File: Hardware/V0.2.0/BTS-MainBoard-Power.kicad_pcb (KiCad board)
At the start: 4 copper layers, 100 x 100 mm, 62 parts, among them J10 PeCon, J11 PeCon, J12 FanConn, J13 FanConn, J14 FanConn, J15 FanConn, J16 FanConn, J17 FanConn, J18 FanConn, J19 FanConn, J3 LogicBoardConnector, J4 PeCon, J5 PeCon, J6 PeCon, J7 PeCon, J8 PeCon, J9 PeCon, Q1 DMG3418L, Q2 NTMFS5H419NL, Q3 NTMFS5H419NL, Q4 NTMFS5H419NL, Q5 NTMFS5H419NL, U1 LM5109BMA, U2 LM5109BMA

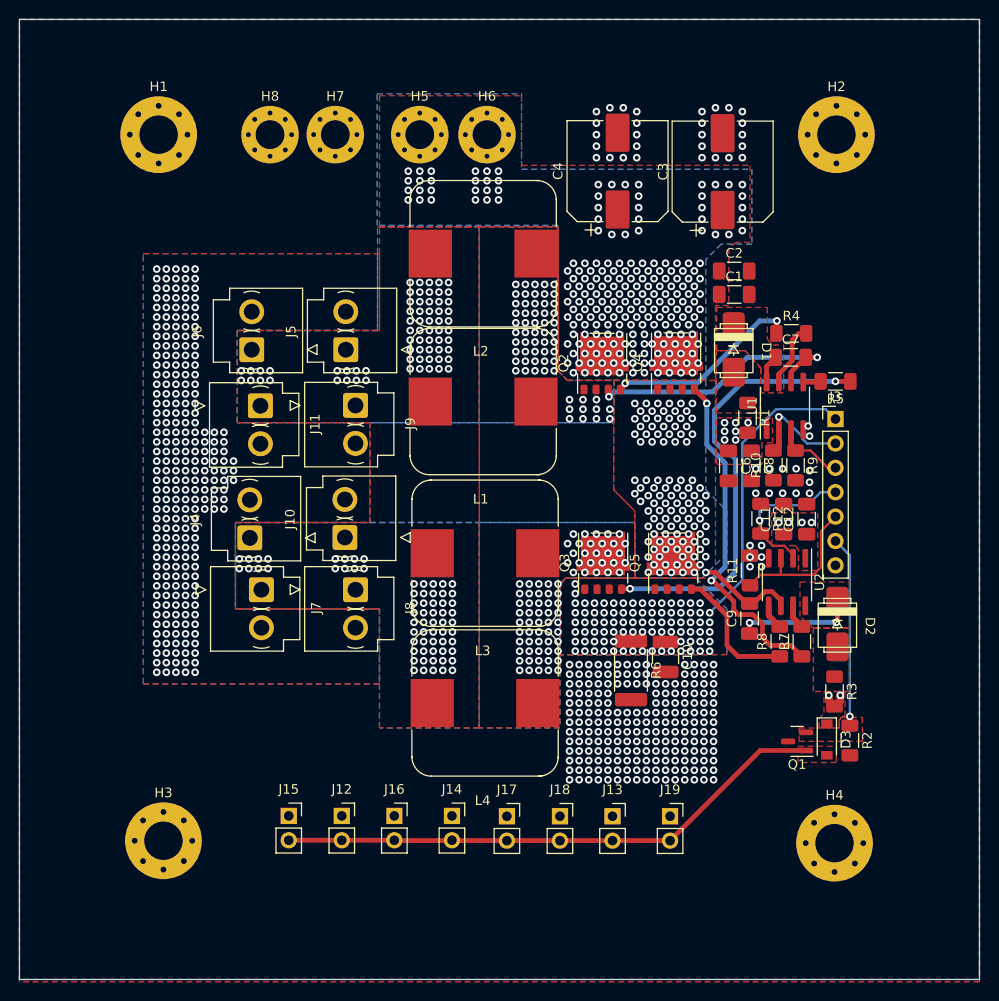
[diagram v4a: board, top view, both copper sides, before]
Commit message: Redid edge cuts
Signed-off-by: bebenlebricolo <benoittarrade@hotmail.fr>
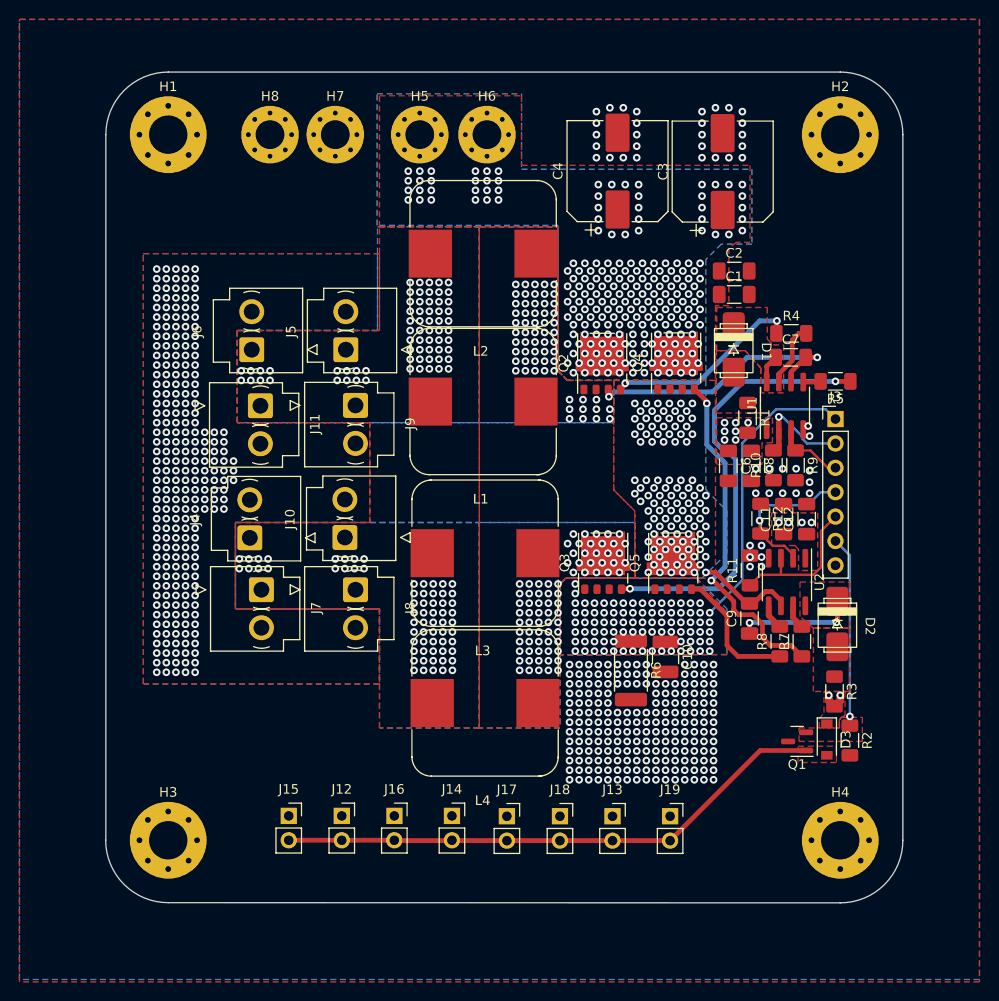
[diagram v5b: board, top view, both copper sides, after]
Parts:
- moved H1 1.00 mm to (114.0, 49.0)
- moved H4 0.67 mm to (184.0, 122.5)
- moved H3 0.50 mm to (114.0, 122.5)
- moved H2 0.40 mm to (184.0, 49.0)
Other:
- board size 100 x 100 mm -> 83 x 86.5 mm
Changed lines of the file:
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@@
   )
   (footprint "MountingHole:MountingHole_4mm_Pad_Via" (layer "F.Cu")
-    (at 183.4 122.8)
+    (at 184 122.5)
     (descr "Mounting Hole 4mm")
     (tags "mounting hole 4mm")
@@
   )
   (footprint "MountingHole:MountingHole_4mm_Pad_Via" (layer "F.Cu")
-    (at 183.6 49)
+    (at 184 49)
     (descr "Mounting Hole 4mm")
     (tags "mounting hole 4mm")
@@
   )
   (footprint "MountingHole:MountingHole_4mm_Pad_Via" (layer "F.Cu")
-    (at 113.5 122.55)
+    (at 114 122.5)
     (descr "Mounting Hole 4mm")
     (tags "mounting hole 4mm")
@@
   )
   (footprint "MountingHole:MountingHole_4mm_Pad_Via" (layer "F.Cu")
-    (at 113 49)
+    (at 114 49)
     (descr "Mounting Hole 4mm")
     (tags "mounting hole 4mm")
@@
       (xy 185.25 77)
     ) (layer "Dwgs.User") (width 0.3) (fill none))
-  (gr_rect (start 98.5 37) (end 198.5 137) (layer "Edge.Cuts") (width 0.05) (fill none))
+  (gr_line (start 184 42.480798) (end 114 42.480798) (layer "Edge.Cuts") (width 0.05))
+  (gr_arc (start 107.5 49) (mid 109.40943 44.390228) (end 114.019202 42.480798) (layer "Edge.Cuts") (width 0.05))
+  (gr_arc (start 184 42.480798) (mid 188.609772 44.390228) (end 190.519202 49) (layer "Edge.Cuts") (width 0.05))
+  (gr_arc (start 190.519202 122.5) (mid 188.609772 127.109772) (end 184 129.019202) (layer "Edge.Cuts") (width 0.05))
+  (gr_arc (start 114 129) (mid 109.390228 127.09057) (end 107.480798 122.480798) (layer "Edge.Cuts") (width 0.05))
+  (gr_line (start 190.519202 49) (end 190.519202 122.5) (layer "Edge.Cuts") (width 0.05))
+  (gr_line (start 107.5 49) (end 107.5 122.5) (layer "Edge.Cuts") (width 0.05))
+  (gr_line (start 114 129) (end 184 129.019202) (layer "Edge.Cuts") (width 0.05))
   (gr_text "Logic board avr bounding area" (at 155.75 63.5) (layer "Dwgs.User")
     (effects (font (size 2.5 2.5) (thickness 0.4)))

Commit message: Improved a bit tracks
Signed-off-by: bebenlebricolo <benoittarrade@hotmail.fr>
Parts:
- moved L1 0.20 mm to (146.8, 77.0)
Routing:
- net /AHO_Sig: track 10.9 -> 9.65 mm
- net /VSense: track 30.7 -> 29.7 mm
- net /HBridge/ALO_Gate: track 46.0 -> 45.1 mm
- net /HBridge/BHO_Gate: track 35.9 -> 35.3 mm
- net GND: vias 241 -> 242

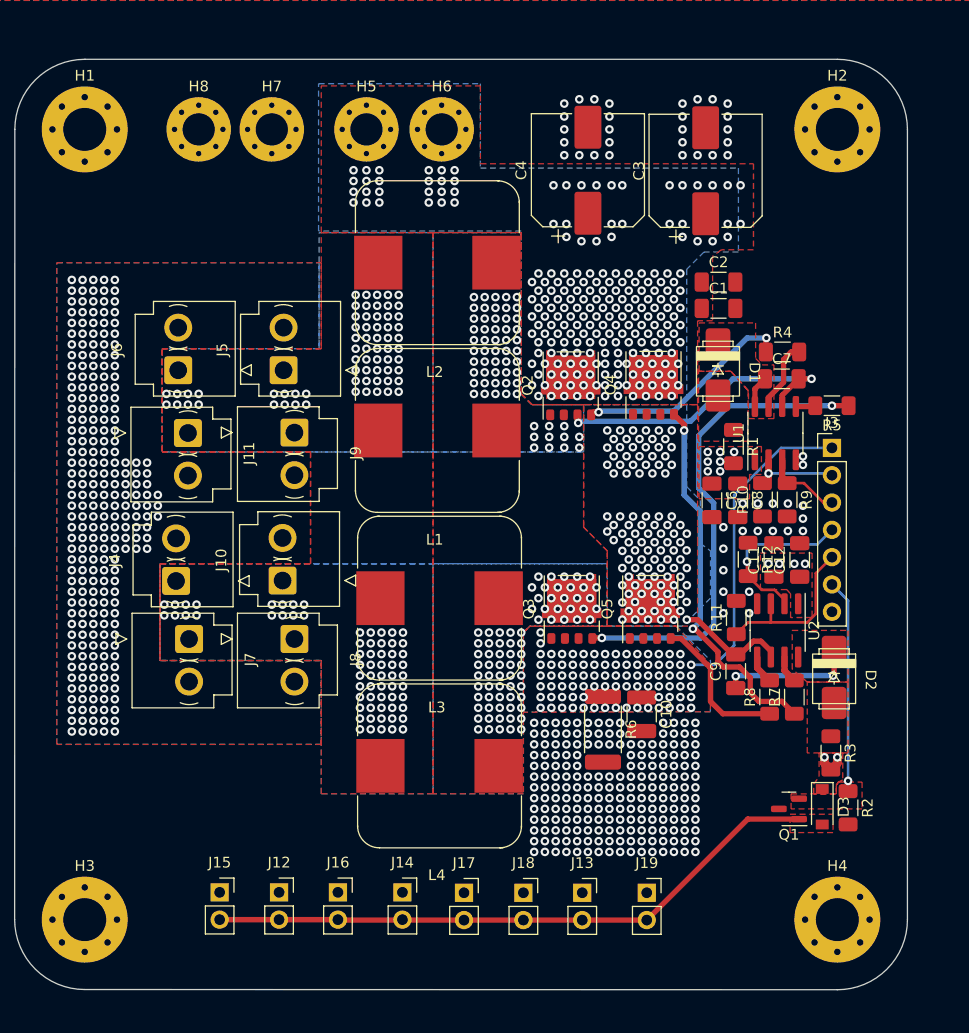
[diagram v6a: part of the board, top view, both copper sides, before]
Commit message: Updated the board with logo and silkscreen improvements
Signed-off-by: bebenlebricolo <benoittarrade@hotmail.fr>
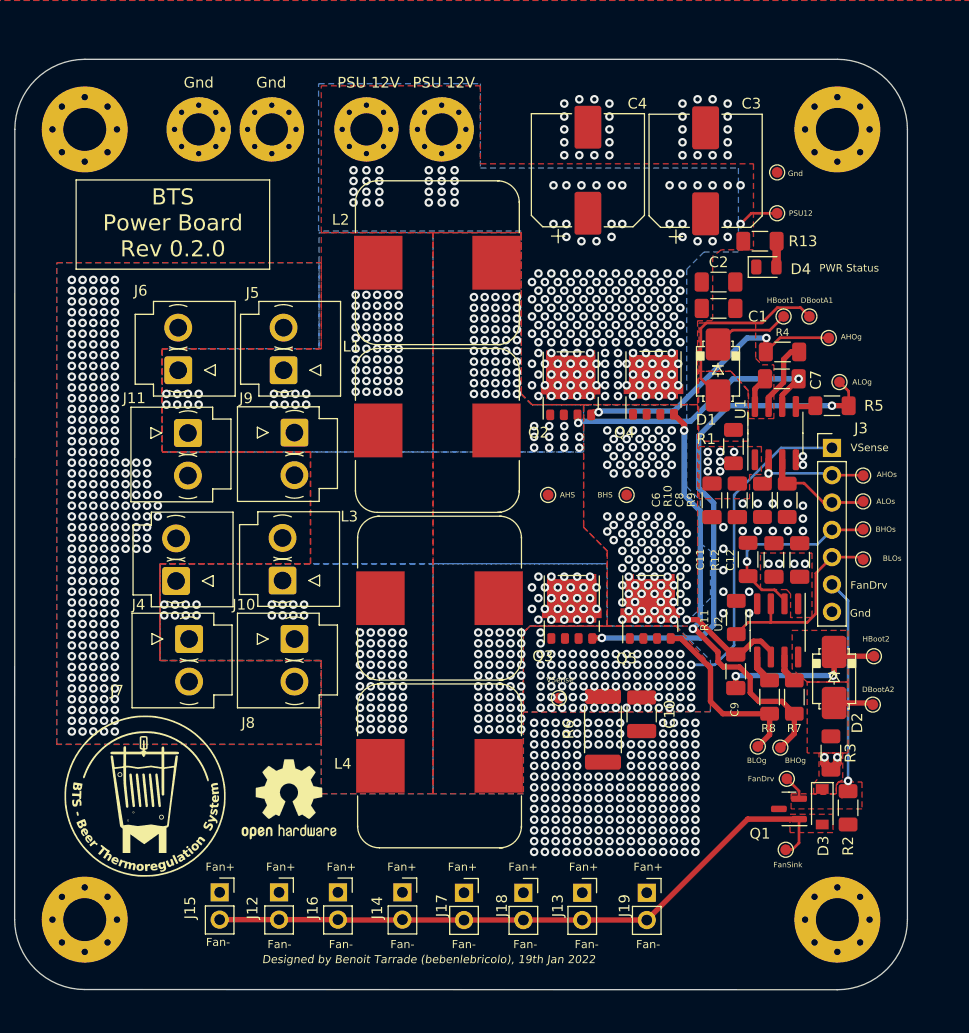
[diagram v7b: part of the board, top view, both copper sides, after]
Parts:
- added D4: LED, Diode_SMD:D_0805_2012Metric, F.Cu at (177.4, 61.8)
- added G***: LOGO, BTS-MainBoard-Power:BTS-LogoBW-WrappedCircle_15x15mm_silk, F.Cu at (119.6, 111.0)
- added G***: LOGO, BTS-MainBoard-Power:BTS-LogoBW-WrappedCircle_20x20mm_silk, B.Cu at (146.6, 82.6)
- added R13: 1k, Resistor_SMD:R_1206_3216Metric_Pad1.30x1.75mm_HandSolder, F.Cu at (176.8, 59.4)
- added REF**: OSHW-Logo2_9.8x8mm_SilkScreen, Symbol:OSHW-Logo2_9.8x8mm_SilkScreen, F.Cu at (133.0, 111.3)
- added REF**: OSHW-Logo2_14.6x12mm_SilkScreen, Symbol:OSHW-Logo2_14.6x12mm_SilkScreen, B.Cu at (182.4, 59.8)
- added TP1: TestPoint, TestPoint:TestPoint_Pad_D1.0mm, F.Cu at (186.4, 81.2)
- added TP10: TestPoint, TestPoint:TestPoint_Pad_D1.0mm, F.Cu at (176.6, 106.4)
- added TP11: TestPoint, TestPoint:TestPoint_Pad_D1.0mm, F.Cu at (178.7, 106.5)
- added TP12: TestPoint, TestPoint:TestPoint_Pad_D1.0mm, F.Cu at (164.4, 83.0)
- added TP13: TestPoint, TestPoint:TestPoint_Pad_D1.0mm, F.Cu at (187.4, 98.0)
- added TP14: TestPoint, TestPoint:TestPoint_Pad_D1.0mm, F.Cu at (187.3, 102.5)
- added TP15: TestPoint, TestPoint:TestPoint_Pad_D1.0mm, F.Cu at (178.4, 56.8)
- added TP16: TestPoint, TestPoint:TestPoint_Pad_D1.0mm, F.Cu at (178.4, 53.0)
- added TP17: TestPoint, TestPoint:TestPoint_Pad_D1.0mm, F.Cu at (179.3, 109.4)
- added TP18: TestPoint, TestPoint:TestPoint_Pad_D1.0mm, F.Cu at (179.2, 116.0)
- added TP19: TestPoint, TestPoint:TestPoint_Pad_D1.0mm, F.Cu at (158.1, 101.9)
- added TP2: TestPoint, TestPoint:TestPoint_Pad_D1.0mm, F.Cu at (186.4, 83.6)
- added TP3: TestPoint, TestPoint:TestPoint_Pad_D1.0mm, F.Cu at (184.2, 72.5)
- added TP4: TestPoint, TestPoint:TestPoint_Pad_D1.0mm, F.Cu at (183.2, 68.4)
- added TP5: TestPoint, TestPoint:TestPoint_Pad_D1.0mm, F.Cu at (157.1, 83.0)
- added TP6: TestPoint, TestPoint:TestPoint_Pad_D1.0mm, F.Cu at (179.0, 66.4)
- added TP7: TestPoint, TestPoint:TestPoint_Pad_D1.0mm, F.Cu at (181.4, 66.4)
- added TP8: TestPoint, TestPoint:TestPoint_Pad_D1.0mm, F.Cu at (186.4, 86.2)
- added TP9: TestPoint, TestPoint:TestPoint_Pad_D1.0mm, F.Cu at (186.4, 89.0)
- moved R10 0.05 mm to (177.0, 83.5)
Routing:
- net /DBootAnode1: track 0.00 -> 18.1 mm
- net /HBoot1: track 2.97 -> 10.2 mm
- net /HBridge/AHO_Gate: track 20.6 -> 27.0 mm
- net /HBoot2: track 12.4 -> 16.3 mm
- net /Psu12V: track 2.80 -> 6.61 mm
- net /FanSink: track 57.8 -> 61.5 mm
- net /HBridge/BHO_Gate: track 35.3 -> 39.0 mm
- net /DBootAnode2: track 0.00 -> 3.66 mm
- net /HBridge/BLO_Gate: track 13.9 -> 17.4 mm
- net /BLO_Sig: track 15.6 -> 18.6 mm
- net /ALO_Sig: track 7.28 -> 10.2 mm
- net /BHO_Sig: track 15.8 -> 18.7 mm
- net /AHO_Sig: track 9.65 -> 12.3 mm
- net /HBridge/ALO_Gate: track 45.1 -> 47.7 mm
- net Net-(D4-Pad2): track 0.00 -> 2.41 mm
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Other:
- board text added: "AHOg"
- board text added: "AHOs"
- board text added: "AHS"
- board text added: "ALOg"
- board text added: "ALOs"
- board text added: "BHOg"
- board text added: "BHOs"
- board text added: "BHS"
- board text added: "BLOg"
- board text added: "BLOs"
- board text added: "BTS - Beer Thermoregulation System - Power Board -"
- board text added: "BTS Power Board Rev 0.2.0"
- board text added: "DBootA1"
- board text added: "DBootA2"
- board text added: "Designed by Benoit Tarrade (bebenlebricolo), 19th Jan 2022"
- board text added: "Fan+"
- board text added: "Fan-"
- board text added: "FanDrv"
- board text added: "FanSink"
- board text added: "Gnd"
- board text added: "HBoot1"
- board text added: "HBoot2"
- board text added: "PSU 12V"
- board text added: "PSU12"
- board text added: "PWR Status"
- board text added: "Repository link : https://github.com/bebenlebricolo/BTS-MainBoard-Power/"
- board text added: "This board was design to interface with 8 Peltier modules (40x40mm, 12V) and is controlled by the BTS-LogicBoard. Both boards are part of the larger BTS project, which provides a heat exchanger as well. More information can be found at : https://github.com/bebenlebricolo/BeerThermoregulationSystem This board uses a full H bridge configuration in asynchronous mode, in order to statically reverse t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"
- board text added: "VSense"
